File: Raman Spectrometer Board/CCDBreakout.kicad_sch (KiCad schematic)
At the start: 0 parts

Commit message: CCD Connector
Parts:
- added Conn5: Molex_SL_05, symbol MRDT_Connectors:Molex_SL_05
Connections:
- new net +5V: Conn5.1
- new net CLK: Conn5.4
- new net GND: Conn5.5
- new net IN: Conn5.2

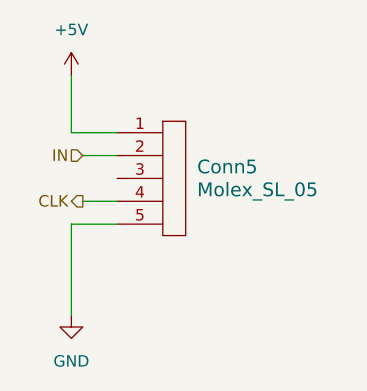
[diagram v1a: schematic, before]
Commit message: ADC Changes + Delete Fan Connector
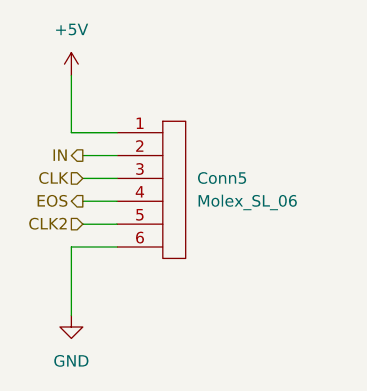
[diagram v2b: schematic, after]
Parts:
- removed Conn5: Molex_SL_05, symbol MRDT_Connectors:Molex_SL_05
- added Conn5: Molex_SL_06, symbol MRDT_Connectors:Molex_SL_06
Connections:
- net +5V: now also Conn5.1
- net CLK: now also Conn5.3
- net GND: now also Conn5.6
- net IN: now also Conn5.2
- new net CLK2: Conn5.5
- new net EOS: Conn5.4
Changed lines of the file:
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@@
 	(wire
 		(pts
-			(xy 154.94 100.33) (xy 158.75 100.33)
+			(xy 154.94 97.79) (xy 158.75 97.79)
+		)
+		(stroke
+			(width 0)
+			(type default)
+		)
+	)
+	(wire
+		(pts
+			(xy 153.67 113.03) (xy 153.67 105.41)
+		)
+		(stroke
+			(width 0)
+			(type default)
+		)
+	)
+	(wire
+		(pts
+			(xy 153.67 105.41) (xy 158.75 105.41)
 		)
 		(stroke
@@
 	(wire
 		(pts
+			(xy 154.94 100.33) (xy 158.75 100.33)
+		)
+		(stroke
+			(width 0)
+			(type default)
+		)
+	)
+	(wire
+		(pts
 			(xy 154.94 95.25) (xy 158.75 95.25)
 		)
@@
 	(wire
 		(pts
-			(xy 153.67 113.03) (xy 153.67 102.87)
+			(xy 154.94 102.87) (xy 158.75 102.87)
 		)
 		(stroke
@@
 		)
 	)
-	(wire
-		(pts
-			(xy 153.67 102.87) (xy 158.75 102.87)
-		)
-		(stroke
-			(width 0)
-			(type default)
+	(hierarchical_label "CLK2"
+		(shape input)
+		(at 154.94 102.87 180)
+		(effects
+			(font
+				(size 1.27 1.27)
+			)
+			(justify right)
 		)
 	)
 	(hierarchical_label "IN"
-		(shape input)
+		(shape output)
 		(at 154.94 95.25 180)
 		(effects
@@
 	)
 	(hierarchical_label "CLK"
+		(shape input)
+		(at 154.94 97.79 180)
+		(effects
+			(font
+				(size 1.27 1.27)
+			)
+			(justify right)
+		)
+	)
+	(hierarchical_label "EOS"
 		(shape output)
 		(at 154.94 100.33 180)
@@
 	)
 	(symbol
-		(lib_id "MRDT_Connectors:Molex_SL_05")
-		(at 163.83 104.14 0)
+		(lib_id "MRDT_Connectors:Molex_SL_06")
+		(at 163.83 106.68 0)
 		(unit 1)
 		(exclude_from_sim no)
@@
 		(fields_autoplaced yes)
 		(property "Reference" "Conn5"
-			(at 167.64 96.5199 0)
+			(at 167.64 97.7899 0)
 			(effects
 				(font
-					(size 1.524 1.524)
+					(size 1.27 1.27)
 				)
 				(justify left)
 			)
 		)
-		(property "Value" "Molex_SL_05"
-			(at 167.64 99.0599 0)
+		(property "Value" "Molex_SL_06"
+			(at 167.64 100.3299 0)
 			(effects
 				(font
-					(size 1.524 1.524)
+					(size 1.27 1.27)
 				)
 				(justify left)
@@
 		)
 		(property "Footprint" ""
-			(at 163.83 104.14 0)
-			(effects
-				(font
-					(size 1.524 1.524)
-				)
-				(hide yes)
-			)
-		)
-		(property "Datasheet" ""
-			(at 163.83 104.14 0)
-			(effects
-				(font
-					(size 1.524 1.524)
-				)
-				(hide yes)
-			)
-		)
-		(property "Description" ""
-			(at 163.83 104.14 0)
+			(at 158.75 102.87 0)
 			(effects
 				(font
@@
 			)
 		)
-		(pin "1"
+		(property "Datasheet" ""
+			(at 158.75 102.87 0)
+			(effects
+				(font
+					(size 1.27 1.27)
+				)
+				(hide yes)
+			)
+		)
+		(property "Description" ""
+			(at 158.75 102.87 0)
+			(effects
+				(font
+					(size 1.27 1.27)
+				)
+				(hide yes)
+			)
+		)
+		(pin "5"
+		)
+		(pin "3"
 		)
 		(pin "2"
 		)
-		(pin "3"
+		(pin "1"
+		)
+		(pin "6"
 		)
 		(pin "4"
 		)
-		(pin "5"
-		)
 		(instances

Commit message: ST and EOS Pin Connections
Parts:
- removed Conn5: Molex_SL_06, symbol MRDT_Connectors:Molex_SL_06
- added Conn5: Molex_uF_S_07, MRDT_Connectors:MOLEX_uF_S_07_Horizontal, symbol MRDT_Connectors:Molex_uF_S_07
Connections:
- net +5V: now also Conn5.1
- net CLK: now also Conn5.3
- net CLK2: now also Conn5.6
- net EOS: now also Conn5.4
- net GND: now also Conn5.7
- net IN: now also Conn5.2
- new net ST: Conn5.5
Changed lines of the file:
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@@
+	(wire
+		(pts
+			(xy 154.94 102.87) (xy 158.75 102.87)
+		)
+		(stroke
+			(width 0)
+			(type default)
+		)
+	)
 	(wire
 		(pts
@@
 	(wire
 		(pts
-			(xy 153.67 113.03) (xy 153.67 105.41)
-		)
-		(stroke
-			(width 0)
-			(type default)
-		)
-	)
-	(wire
-		(pts
-			(xy 153.67 105.41) (xy 158.75 105.41)
+			(xy 153.67 115.57) (xy 153.67 107.95)
 		)
 		(stroke
@@
 	(wire
 		(pts
+			(xy 154.94 105.41) (xy 158.75 105.41)
+		)
+		(stroke
+			(width 0)
+			(type default)
+		)
+	)
+	(wire
+		(pts
 			(xy 154.94 100.33) (xy 158.75 100.33)
 		)
@@
 	(wire
 		(pts
-			(xy 154.94 102.87) (xy 158.75 102.87)
+			(xy 153.67 107.95) (xy 158.75 107.95)
 		)
 		(stroke
@@
 	(hierarchical_label "CLK2"
 		(shape input)
-		(at 154.94 102.87 180)
+		(at 154.94 105.41 180)
 		(effects
 			(font
@@
 		)
 	)
+	(hierarchical_label "ST"
+		(shape input)
+		(at 154.94 102.87 180)
+		(effects
+			(font
+				(size 1.27 1.27)
+			)
+			(justify right)
+		)
+	)
 	(symbol
-		(lib_id "MRDT_Connectors:Molex_SL_06")
-		(at 163.83 106.68 0)
+		(lib_id "MRDT_Connectors:Molex_uF_S_07")
+		(at 163.83 109.22 0)
 		(unit 1)
 		(exclude_from_sim no)
@@
 		(fields_autoplaced yes)
 		(property "Reference" "Conn5"
-			(at 167.64 97.7899 0)
-			(effects
-				(font
-					(size 1.27 1.27)
+			(at 167.64 99.0599 0)
+			(effects
+				(font
+					(size 1.524 1.524)
 				)
 				(justify left)
 			)
 		)
-		(property "Value" "Molex_SL_06"
-			(at 167.64 100.3299 0)
-			(effects
-				(font
-					(size 1.27 1.27)
+		(property "Value" "Molex_uF_S_07"
+			(at 167.64 101.5999 0)
+			(effects
+				(font
+					(size 1.524 1.524)
 				)
 				(justify left)
 			)
 		)
-		(property "Footprint" ""
-			(at 158.75 102.87 0)
-			(effects
-				(font
-					(size 1.27 1.27)
+		(property "Footprint" "MRDT_Connectors:MOLEX_uF_S_07_Horizontal"
+			(at 163.83 104.14 0)
+			(effects
+				(font
+					(size 1.524 1.524)
 				)
 				(hide yes)
@@
 		)
 		(property "Datasheet" ""
-			(at 158.75 102.87 0)
-			(effects
-				(font
-					(size 1.27 1.27)
+			(at 163.83 104.14 0)
+			(effects
+				(font
+					(size 1.524 1.524)
 				)
 				(hide yes)
@@
 		)
 		(property "Description" ""
-			(at 158.75 102.87 0)
+			(at 163.83 109.22 0)
 			(effects
 				(font
@@
 		(pin "5"
 		)
+		(pin "2"
+		)
+		(pin "4"
+		)
+		(pin "7"
+		)
+		(pin "1"
+		)
+		(pin "6"
+		)
 		(pin "3"
-		)
-		(pin "2"
-		)
-		(pin "1"
-		)
-		(pin "6"
-		)
-		(pin "4"
 		)
 		(instances
@@
 	(symbol
 		(lib_id "power:GND")
-		(at 153.67 113.03 0)
+		(at 153.67 115.57 0)
 		(unit 1)
 		(exclude_from_sim no)
@@
 		(fields_autoplaced yes)
 		(property "Reference" "#PWR027"
-			(at 153.67 119.38 0)
+			(at 153.67 121.92 0)
 			(effects
 				(font
@@
 		)
 		(property "Value" "GND"
-			(at 153.67 118.11 0)
+			(at 153.67 120.65 0)
 			(effects
 				(font
@@
 		)
 		(property "Footprint" ""
-			(at 153.67 113.03 0)
+			(at 153.67 115.57 0)
 			(effects
 				(font
@@
 		)
 		(property "Datasheet" ""
-			(at 153.67 113.03 0)
+			(at 153.67 115.57 0)
 			(effects
 				(font
@@
 		)
 		(property "Description" "Power symbol creates a global label with name \"GND\" , ground"
-			(at 153.67 113.03 0)
-			(effects
-				(font
+			(at 153.67 115.57 0)
+			(effects
+				(font

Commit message: Page Consolidation
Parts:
- added Q3, Q7: BSS138, Package_TO_SOT_SMD:SOT-23, symbol Transistor_FET:BSS138
- added R11, R13: 4.7k, Resistor_SMD:R_0201_0603Metric_Pad0.64x0.40mm_HandSolder, symbol Device:R_US
- added R12, R14: 2.2k, Resistor_SMD:R_0201_0603Metric_Pad0.64x0.40mm_HandSolder, symbol Device:R_US
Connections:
- net +5V: now also R11.1, R13.1
- net CLK: no longer names the net of Conn5.3
- net CLK: now also Q7.3 (D), R13.2
- net CLK2: no longer names the net of Conn5.6
- net CLK2: now also Q3.3 (D), R11.2
- new net: Q3.1 (G), R12.2
- new net: Q7.1 (G), R14.2
- new net +3V3: R12.1, R14.1
- new net ADC_CLK_3V3: Q3.2 (S)
- new net CCD_CLK_3V3: Q7.2 (S)

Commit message: High Side Fan Connector
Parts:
- removed Conn5: Molex_uF_S_07, MRDT_Connectors:MOLEX_uF_S_07_Horizontal, symbol MRDT_Connectors:Molex_uF_S_07
- added Conn3: Molex_SL_07, symbol MRDT_Connectors:Molex_SL_07
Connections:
- net +5V: now also Conn3.1
- net EOS: now also Conn3.4
- net GND: now also Conn3.7
- net IN: now also Conn3.2
- net ST: now also Conn3.5
- net at Q7.3 (D), R13.2: now also Conn3.3
- net at Q3.3 (D), R11.2: now also Conn3.6
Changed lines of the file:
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@@
+	)
+	(symbol
+		(lib_id "MRDT_Connectors:Molex_SL_07")
+		(at 163.83 109.22 0)
+		(unit 1)
+		(exclude_from_sim no)
+		(in_bom yes)
+		(on_board yes)
+		(dnp no)
+		(fields_autoplaced yes)
+		(property "Reference" "Conn3"
+			(at 167.64 99.0599 0)
+			(effects
+				(font
+					(size 1.524 1.524)
+				)
+				(justify left)
+			)
+		)
+		(property "Value" "Molex_SL_07"
+			(at 167.64 101.5999 0)
+			(effects
+				(font
+					(size 1.524 1.524)
+				)
+				(justify left)
+			)
+		)
+		(property "Footprint" ""
+			(at 163.83 104.14 0)
+			(effects
+				(font
+					(size 1.524 1.524)
+				)
+				(hide yes)
+			)
+		)
+		(property "Datasheet" ""
+			(at 163.83 104.14 0)
+			(effects
+				(font
+					(size 1.524 1.524)
+				)
+				(hide yes)
+			)
+		)
+		(property "Description" ""
+			(at 163.83 109.22 0)
+			(effects
+				(font
+					(size 1.27 1.27)
+				)
+				(hide yes)
+			)
+		)
+		(pin "7"
+		)
+		(pin "2"
+		)
+		(pin "3"
+		)
+		(pin "4"
+		)
+		(pin "5"
+		)
+		(pin "1"
+		)
+		(pin "6"
+		)
+		(instances
+			(project ""
+				(path "/ab487c59-f066-48f5-a383-99e8eaf806bf/3c339d9b-500e-4752-bc41-2adbdf3d2bf6"
+					(reference "Conn3")
+					(unit 1)
+				)
+			)
+		)
 	)
 	(symbol
@@
 					(unit 1)
 				)
-			)
-		)
-	)
-	(symbol
-		(lib_id "MRDT_Connectors:Molex_uF_S_07")
-		(at 163.83 109.22 0)
-		(unit 1)
-		(exclude_from_sim no)
-		(in_bom yes)
-		(on_board yes)
-		(dnp no)
-		(fields_autoplaced yes)
-		(property "Reference" "Conn5"
-			(at 167.64 99.0599 0)
-			(effects
-				(font
-					(size 1.524 1.524)
-				)
-				(justify left)
-			)
-		)
-		(property "Value" "Molex_uF_S_07"
-			(at 167.64 101.5999 0)
-			(effects
-				(font
-					(size 1.524 1.524)
-				)
-				(justify left)
-			)
-		)
-		(property "Footprint" "MRDT_Connectors:MOLEX_uF_S_07_Horizontal"
-			(at 163.83 104.14 0)
-			(effects
-				(font
-					(size 1.524 1.524)
-				)
-				(hide yes)
-			)
-		)
-		(property "Datasheet" ""
-			(at 163.83 104.14 0)
-			(effects
-				(font
-					(size 1.524 1.524)
-				)
-				(hide yes)
-			)
-		)
-		(property "Description" ""
-			(at 163.83 109.22 0)
-			(effects
-				(font
-					(size 1.27 1.27)
-				)
-				(hide yes)
-			)
-		)
-		(pin "5"
-		)
-		(pin "2"
-		)
-		(pin "4"
-		)
-		(pin "7"
-		)
-		(pin "1"
-		)
-		(pin "6"
-		)
-		(pin "3"
-		)
-		(instances
-			(project ""
-				(path "/ab487c59-f066-48f5-a383-99e8eaf806bf/3c339d9b-500e-4752-bc41-2adbdf3d2bf6"
-					(reference "Conn5")
-					(unit 1)
-				)

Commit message: Added 3.3v to the CCD
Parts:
- removed Conn3: Molex_SL_07, symbol MRDT_Connectors:Molex_SL_07
- added Conn3: Molex_SL_08, symbol MRDT_Connectors:Molex_SL_08
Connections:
- net +3V3: now also Conn3.1
- net +5V: now also Conn3.2
- net EOS: now also Conn3.5
- net GND: now also Conn3.8
- net IN: now also Conn3.3
- net ST: now also Conn3.6
- net at Q7.3 (D), R13.2: now also Conn3.4
- net at Q3.3 (D), R11.2: now also Conn3.7
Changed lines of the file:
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@@
+	(wire
+		(pts
+			(xy 148.59 90.17) (xy 158.75 90.17)
+		)
+		(stroke
+			(width 0)
+			(type default)
+		)
+	)
+	(wire
+		(pts
+			(xy 148.59 80.01) (xy 148.59 90.17)
+		)
+		(stroke
+			(width 0)
+			(type default)
+		)
+	)
 	(wire
 		(pts
@@
 	)
 	(symbol
-		(lib_id "MRDT_Connectors:Molex_SL_07")
+		(lib_id "MRDT_Connectors:Molex_SL_08")
 		(at 163.83 109.22 0)
 		(unit 1)
@@
 		(fields_autoplaced yes)
 		(property "Reference" "Conn3"
-			(at 167.64 99.0599 0)
+			(at 167.64 97.7899 0)
 			(effects
 				(font
@@
 			)
 		)
-		(property "Value" "Molex_SL_07"
-			(at 167.64 101.5999 0)
+		(property "Value" "Molex_SL_08"
+			(at 167.64 100.3299 0)
 			(effects
 				(font
@@
 		)
 		(property "Footprint" ""
-			(at 163.83 104.14 0)
+			(at 163.83 101.6 0)
 			(effects
 				(font
@@
 		)
 		(property "Datasheet" ""
-			(at 163.83 104.14 0)
+			(at 163.83 101.6 0)
 			(effects
 				(font
@@
 			)
 		)
+		(pin "2"
+		)
+		(pin "6"
+		)
+		(pin "5"
+		)
+		(pin "1"
+		)
+		(pin "8"
+		)
+		(pin "4"
+		)
 		(pin "7"
 		)
-		(pin "2"
-		)
 		(pin "3"
 		)
-		(pin "4"
-		)
-		(pin "5"
-		)
-		(pin "1"
-		)
-		(pin "6"
-		)
-		(instances
-			(project ""
+		(instances
+			(project "RamanSpectrometerBoard"
 				(path "/ab487c59-f066-48f5-a383-99e8eaf806bf/3c339d9b-500e-4752-bc41-2adbdf3d2bf6"
 					(reference "Conn3")
@@
 					(unit 1)
 				)
+			)
+		)
+	)
+	(symbol
+		(lib_id "power:+3V3")
+		(at 148.59 80.01 0)
+		(unit 1)
+		(exclude_from_sim no)
+		(in_bom yes)
+		(on_board yes)
+		(dnp no)
+		(fields_autoplaced yes)
+		(property "Reference" "#PWR040"
+			(at 148.59 83.82 0)
+			(effects
+				(font
+					(size 1.27 1.27)
+				)
+				(hide yes)
+			)
+		)
+		(property "Value" "+3V3"
+			(at 148.59 74.93 0)
+			(effects
+				(font
+					(size 1.27 1.27)
+				)
+			)
+		)
+		(property "Footprint" ""
+			(at 148.59 80.01 0)
+			(effects
+				(font
+					(size 1.27 1.27)
+				)
+				(hide yes)
+			)
+		)
+		(property "Datasheet" ""
+			(at 148.59 80.01 0)
+			(effects
+				(font
+					(size 1.27 1.27)
+				)
+				(hide yes)
+			)
+		)
+		(property "Description" "Power symbol creates a global label with name \"+3V3\""
+			(at 148.59 80.01 0)
+			(effects
+				(font
+					(size 1.27 1.27)
+				)
+				(hide yes)
+			)
+		)
+		(pin "1"
+		)
+		(instances
+			(project ""
+				(path "/ab487c59-f066-48f5-a383-99e8eaf806bf/3c339d9b-500e-4752-bc41-2adbdf3d2bf6"
+					(reference "#PWR040")
+					(unit 1)
+				)

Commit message: Draft layout design
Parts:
- Conn3: footprint (none) -> MRDT_Connectors:MOLEX_SL_08_Horizontal
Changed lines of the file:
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@@
 			)
 		)
-		(property "Footprint" ""
+		(property "Footprint" "MRDT_Connectors:MOLEX_SL_08_Horizontal"
 			(at 163.83 101.6 0)
 			(effects

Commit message: Fix Layout Issues
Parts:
- Conn3: footprint MRDT_Connectors:MOLEX_SL_08_Horizontal -> MRDT_Connectors:MOLEX_SL_08_Vertical
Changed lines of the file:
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@@
 			)
 		)
-		(property "Footprint" "MRDT_Connectors:MOLEX_SL_08_Horizontal"
+		(property "Footprint" "MRDT_Connectors:MOLEX_SL_08_Vertical"
 			(at 163.83 101.6 0)
 			(effects
